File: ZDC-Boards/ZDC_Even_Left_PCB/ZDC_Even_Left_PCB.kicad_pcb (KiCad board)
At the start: 2 copper layers, 202.6 x 643 mm, 103 parts

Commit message: Updated ZDC connectors to pad connections, v2.0
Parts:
- removed REF** (x2): PinHeader_2x25_P1.27mm_Horizontal, Connector_PinHeader_1.27mm:PinHeader_2x25_P1.27mm_Horizontal
- added J1: TE_5-104895-5_AMPMODU_50-50_2x25_P1.27mm_Horizontal_SMD, TE_AMPMODU:TE_5-104895-5_AMPMODU_50-50_2x25_P1.27mm_Horizontal_SMD, F.Cu at (48.8, -634.4)
- added J2: TE_5-104895-5_AMPMODU_50-50_2x25_P1.27mm_Horizontal_SMD, TE_AMPMODU:TE_5-104895-5_AMPMODU_50-50_2x25_P1.27mm_Horizontal_SMD, F.Cu at (146.4, -634.4)
- #MK1, #MK2: renamed from REF**20; footprint SiPM:S14160-1315PS_dimple_silkscreen_with_capacitor -> SiPM:S14160-1315PS_silkscreen_marker
- C0, C1, C10, C11, C12, C13, C14, C15, C16, C17, C18, C19, C2, C20, C21, C22, C23, C24, C25, C26, C27, C28, C29, C3, C30, C31, C32, C33, C34, C35, C36, C37, C38, C39, C4, C40, C41, C42, C43, C44, C45, C46, C47, C5, C6, C7, C8, C9: renamed from 10 nF
- renumbered REF**20 to D0, REF**20 to D1, REF**20 to D10, REF**20 to D11, REF**20 to D12, REF**20 to D13, REF**20 to D14, REF**20 to D15, REF**20 to D16, REF**20 to D17, REF**20 to D18, REF**20 to D19, REF**20 to D2, REF**20 to D20, REF**20 to D21, REF**20 to D22, REF**20 to D23, REF**20 to D24, REF**20 to D25, REF**20 to D26, REF**20 to D27, REF**20 to D28, REF**20 to D29, REF**20 to D3, REF**20 to D30, REF**20 to D31, REF**20 to D32, REF**20 to D33, REF**20 to D34, REF**20 to D35, REF**20 to D36, REF**20 to D37, REF**20 to D38, REF**20 to D39, REF**20 to D4, REF**20 to D40, REF**20 to D41, REF**20 to D42, REF**20 to D43, REF**20 to D44, REF**20 to D45, REF**20 to D46, REF**20 to D47, REF**20 to D5, REF**20 to D6, REF**20 to D7, REF**20 to D8, REF**20 to D9, REF** to J3, REF** to J4
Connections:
- C24 pad 1: K0 -> K24
- C25 pad 1: K1 -> K25
- C26 pad 1: K2 -> K26
- C27 pad 1: K3 -> K27
- C28 pad 1: K4 -> K28
- C29 pad 1: K5 -> K29
- C30 pad 1: K6 -> K30
- C31 pad 1: K7 -> K31
- C32 pad 1: K8 -> K32
- C33 pad 1: K9 -> K33
- C34 pad 1: K10 -> K34
- C35 pad 1: K11 -> K35
- C36 pad 1: K12 -> K36
- C37 pad 1: K13 -> K37
- C38 pad 1: K14 -> K38
- C39 pad 1: K15 -> K39
- C40 pad 1: K16 -> K40
- C41 pad 1: K17 -> K41
- C42 pad 1: K18 -> K42
- C43 pad 1: K19 -> K43
- C44 pad 1: K20 -> K44
- C45 pad 1: K21 -> K45
- C46 pad 1: K22 -> K46
- C47 pad 1: K23 -> K47
- D0 pad : LK -> LK1
- D0 pad 7: (no net) -> K0
- D0 pad 8: (no net) -> A0
- D0 pad 9: LA -> LA1
- D1 pad : LK -> LK1
- D1 pad 7: (no net) -> K1
- D1 pad 8: (no net) -> A1
- D1 pad 9: LA -> LA1
- D10 pad : LK -> LK1
- D10 pad 7: (no net) -> K10
- D10 pad 8: (no net) -> A10
- D10 pad 9: LA -> LA1
- D11 pad : LK -> LK1
- D11 pad 7: (no net) -> K11
- D11 pad 8: (no net) -> A11
- D11 pad 9: LA -> LA1
- D12 pad : LK -> LK1
- D12 pad 9: LA -> LA1
- D13 pad : LK -> LK1
- D13 pad 7: (no net) -> K13
- D13 pad 8: (no net) -> A13
- D13 pad 9: LA -> LA1
- D14 pad : LK -> LK1
- D14 pad 7: (no net) -> K14
- D14 pad 8: (no net) -> A14
- D14 pad 9: LA -> LA1
- D15 pad : LK -> LK1
- D15 pad 7: (no net) -> K15
- D15 pad 8: (no net) -> A15
- D15 pad 9: LA -> LA1
- D16 pad : LK -> LK1
- D16 pad 7: (no net) -> K16
- D16 pad 8: (no net) -> A16
- D16 pad 9: LA -> LA1
- D17 pad : LK -> LK1
- D17 pad 7: (no net) -> K17
- D17 pad 9: LA -> LA1
- D18 pad : LK -> LK1
- D18 pad 7: (no net) -> K18
- D18 pad 8: (no net) -> A18
- D18 pad 9: LA -> LA1
- D19 pad : LK -> LK1
- D19 pad 7: (no net) -> K19
- D19 pad 8: (no net) -> A19
- D19 pad 9: LA -> LA1
- D2 pad : LK -> LK1
- D2 pad 7: (no net) -> K2
- D2 pad 8: (no net) -> A2
- D2 pad 9: LA -> LA1
- D20 pad : LK -> LK1
- D20 pad 7: (no net) -> K20
- D20 pad 8: (no net) -> A20
- D20 pad 9: LA -> LA1
- D21 pad : LK -> LK1
- D21 pad 7: (no net) -> K21
- D21 pad 8: (no net) -> A21
- D21 pad 9: LA -> LA1
- D22 pad : LK -> LK1
- D22 pad 7: (no net) -> K22
- D22 pad 8: (no net) -> A22
- D22 pad 9: LA -> LA1
- D23 pad : LK -> LK1
- D23 pad 7: (no net) -> K23
- D23 pad 8: (no net) -> A23
- D23 pad 9: LA -> LA1
- D24 pad : LK -> LK2
- D24 pad 7: (no net) -> K24
- D24 pad 8: (no net) -> A24
- D24 pad 9: LA -> LA2
- D25 pad : LK -> LK2
- D25 pad 7: (no net) -> K25
- D25 pad 8: (no net) -> A25
- D25 pad 9: LA -> LA2
- D26 pad : LK -> LK2
- D26 pad 7: (no net) -> K26
- D26 pad 8: (no net) -> A26
- D26 pad 9: LA -> LA2
- D27 pad : LK -> LK2
- D27 pad 7: (no net) -> K27
- D27 pad 8: (no net) -> A27
- D27 pad 9: LA -> LA2
- D28 pad : LK -> LK2
- D28 pad 7: (no net) -> K28
- D28 pad 8: (no net) -> A28
- D28 pad 9: LA -> LA2
- D29 pad : LK -> LK2
- D29 pad 7: (no net) -> K29
- D29 pad 8: A5 -> A29
- D29 pad 9: LA -> LA2
- D3 pad : LK -> LK1
- D3 pad 7: (no net) -> K3
- D3 pad 8: (no net) -> A3
- D3 pad 9: LA -> LA1
- D30 pad : LK -> LK2
- D30 pad 7: (no net) -> K30
- D30 pad 8: (no net) -> A30
- D30 pad 9: LA -> LA2
- D31 pad : LK -> LK2
- D31 pad 7: (no net) -> K31
- D31 pad 8: (no net) -> A31
- D31 pad 9: LA -> LA2
- D32 pad : LK -> LK2
- D32 pad 7: (no net) -> K32
- D32 pad 8: (no net) -> A32
- D32 pad 9: LA -> LA2
- D33 pad : LK -> LK2
- D33 pad 7: (no net) -> K33
- D33 pad 8: (no net) -> A33
- D33 pad 9: LA -> LA2
- D34 pad : LK -> LK2
- D34 pad 7: (no net) -> K34
- D34 pad 8: (no net) -> A34
- D34 pad 9: LA -> LA2
- D35 pad : LK -> LK2
- D35 pad 7: (no net) -> K35
- D35 pad 8: (no net) -> A35
- D35 pad 9: LA -> LA2
- D36 pad : LK -> LK2
- D36 pad 7: K12 -> K36
- D36 pad 8: A12 -> A36
- D36 pad 9: LA -> LA2
- D37 pad : LK -> LK2
- D37 pad 7: (no net) -> K37
- D37 pad 8: (no net) -> A37
- D37 pad 9: LA -> LA2
- D38 pad : LK -> LK2
- D38 pad 7: (no net) -> K38
- D38 pad 8: (no net) -> A38
- D38 pad 9: LA -> LA2
- D39 pad : LK -> LK2
- D39 pad 7: (no net) -> K39
- D39 pad 8: (no net) -> A39
- D39 pad 9: LA -> LA2
- D4 pad : LK -> LK1
- D4 pad 7: (no net) -> K4
- D4 pad 8: (no net) -> A4
- D4 pad 9: LA -> LA1
- D40 pad : LK -> LK2
- D40 pad 7: (no net) -> K40
- D40 pad 8: (no net) -> A40
- D40 pad 9: LA -> LA2
- D41 pad : LK -> LK2
- D41 pad 7: (no net) -> K41
- D41 pad 8: A17 -> A41
- D41 pad 9: LA -> LA2
- D42 pad : LK -> LK2
- D42 pad 7: (no net) -> K42
- D42 pad 8: (no net) -> A42
- D42 pad 9: LA -> LA2
- D43 pad : LK -> LK2
- D43 pad 7: (no net) -> K43
- D43 pad 8: (no net) -> A43
- D43 pad 9: LA -> LA2
- D44 pad : LK -> LK2
- D44 pad 7: (no net) -> K44
- D44 pad 8: (no net) -> A44
- D44 pad 9: LA -> LA2
- D45 pad : LK -> LK2
- D45 pad 7: (no net) -> K45
- D45 pad 8: (no net) -> A45
- D45 pad 9: LA -> LA2
- D46 pad : LK -> LK2
- D46 pad 7: (no net) -> K46
- D46 pad 8: (no net) -> A46
- D46 pad 9: LA -> LA2
- D47 pad : LK -> LK2
- D47 pad 7: (no net) -> K47
- D47 pad 8: (no net) -> A47
- D47 pad 9: LA -> LA2
- D5 pad : LK -> LK1
- D5 pad 7: (no net) -> K5
- D5 pad 9: LA -> LA1
- D6 pad : LK -> LK1
- D6 pad 7: (no net) -> K6
- D6 pad 8: (no net) -> A6
- D6 pad 9: LA -> LA1
- D7 pad : LK -> LK1
- D7 pad 7: (no net) -> K7
- D7 pad 8: (no net) -> A7
- D7 pad 9: LA -> LA1
- D8 pad : LK -> LK1
- D8 pad 7: (no net) -> K8
- D8 pad 8: (no net) -> A8
- D8 pad 9: LA -> LA1
- D9 pad : LK -> LK1
- D9 pad 7: (no net) -> K9
- D9 pad 8: (no net) -> A9
- D9 pad 9: LA -> LA1
- J3 pad 1: LA -> LA1
- J3 pad 2: LK -> LK1
- J4 pad 1: LA -> LA2
- J4 pad 2: LK -> LK2
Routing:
- net LK: track 2631.7 -> 0.00 mm, vias 48 -> 0
- net LA: track 2524.0 -> 0.00 mm, vias 4 -> 0
- net LK1: track 0.00 -> 1315.8 mm, vias 0 -> 24
- net LK2: track 0.00 -> 1315.8 mm, vias 0 -> 24
- net LA2: track 0.00 -> 1265.0 mm, vias 0 -> 2
- net LA1: track 0.00 -> 1265.0 mm, vias 0 -> 2
- net A35: track 0.00 -> 657.6 mm
- net A47: track 0.00 -> 655.7 mm
- net A23: track 1310.2 -> 655.7 mm
- net K47: track 0.00 -> 643.2 mm, vias 0 -> 2
- net K23: track 1285.6 -> 643.2 mm, vias 4 -> 2
- net A11: track 1295.7 -> 657.6 mm
- net K11: track 1248.1 -> 622.9 mm, vias 4 -> 2
- net K35: track 0.00 -> 622.9 mm, vias 0 -> 2
- net A46: track 0.00 -> 610.5 mm
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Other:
- board text added: "TE 5-104895-5 (AMPMODU 50/50 R/A SMT)"
- board text added: "ZDC Even Left PCB v2.0 Designed by Sean Preins"
- board text removed: "ZDC Even Left PCB v1.0 Designed by Sean Preins"

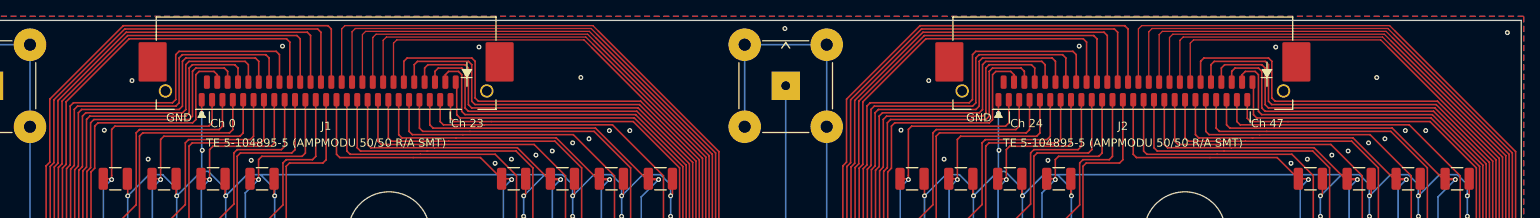
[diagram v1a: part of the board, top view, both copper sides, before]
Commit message: Updated ZDC boards to use new pin connectors that attach to crimped cables
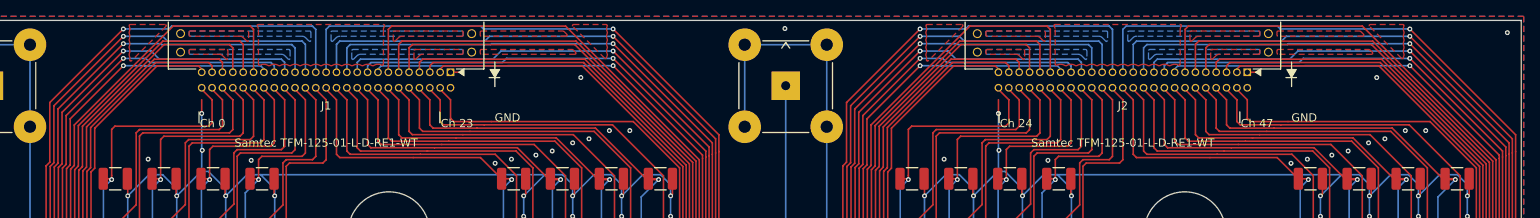
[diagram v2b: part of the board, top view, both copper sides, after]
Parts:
- J1, J2: value TE_5-104895-5_AMPMODU_50-50_2x25_P1.27mm_Horizontal_SMD -> Samtec_TFM-125-01-x-D-RE1-WT_2x25_P1.27mm_Horizontal; footprint TE_AMPMODU:TE_5-104895-5_AMPMODU_50-50_2x25_P1.27mm_Horizontal_SMD -> Samtec_TFM:Samtec_TFM-125-01-x-D-RE1-WT_2x25_P1.27mm_Horizontal
- moved #MK1 3.42 mm to (69.4, -636.0)
- moved #MK2 3.02 mm to (167.0, -636.0)
- moved J1 1.34 mm to (48.8, -635.7), turned to 0 degrees
- moved J2 1.34 mm to (146.4, -635.7), turned to 0 degrees
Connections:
- J1 pad 10: A3 -> K20
- J1 pad 11: K4 -> A19
- J1 pad 12: A4 -> K19
- J1 pad 13: K5 -> A18
- J1 pad 14: A5 -> K18
- J1 pad 15: K6 -> A17
- J1 pad 16: A6 -> K17
- J1 pad 17: K7 -> A16
- J1 pad 18: A7 -> K16
- J1 pad 19: K8 -> A15
- J1 pad 20: A8 -> K15
- J1 pad 21: K9 -> A14
- J1 pad 22: A9 -> K14
- J1 pad 23: K10 -> A13
- J1 pad 24: A10 -> K13
- J1 pad 25: K11 -> A12
- J1 pad 26: A11 -> K12
- J1 pad 27: K12 -> A11
- J1 pad 28: A12 -> K11
- J1 pad 29: K13 -> A10
- J1 pad 3: K0 -> A23
- J1 pad 30: A13 -> K10
- J1 pad 31: K14 -> A9
- J1 pad 32: A14 -> K9
- J1 pad 33: K15 -> A8
- J1 pad 34: A15 -> K8
- J1 pad 35: K16 -> A7
- J1 pad 36: A16 -> K7
- J1 pad 37: K17 -> A6
- J1 pad 38: A17 -> K6
- J1 pad 39: K18 -> A5
- J1 pad 4: A0 -> K23
- J1 pad 40: A18 -> K5
- J1 pad 41: K19 -> A4
- J1 pad 42: A19 -> K4
- J1 pad 43: K20 -> A3
- J1 pad 44: A20 -> K3
- J1 pad 45: K21 -> A2
- J1 pad 46: A21 -> K2
- J1 pad 47: K22 -> A1
- J1 pad 48: A22 -> K1
- J1 pad 49: K23 -> A0
- J1 pad 5: K1 -> A22
- J1 pad 50: A23 -> K0
- J1 pad 6: A1 -> K22
- J1 pad 7: K2 -> A21
- J1 pad 8: A2 -> K21
- J1 pad 9: K3 -> A20
- J2 pad 10: A27 -> K44
- J2 pad 11: K28 -> A43
- J2 pad 12: A28 -> K43
- J2 pad 13: K29 -> A42
- J2 pad 14: A29 -> K42
- J2 pad 15: K30 -> A41
- J2 pad 16: A30 -> K41
- J2 pad 17: K31 -> A40
- J2 pad 18: A31 -> K40
- J2 pad 19: K32 -> A39
- J2 pad 20: A32 -> K39
- J2 pad 21: K33 -> A38
- J2 pad 22: A33 -> K38
- J2 pad 23: K34 -> A37
- J2 pad 24: A34 -> K37
- J2 pad 25: K35 -> A36
- J2 pad 26: A35 -> K36
- J2 pad 27: K36 -> A35
- J2 pad 28: A36 -> K35
- J2 pad 29: K37 -> A34
- J2 pad 3: K24 -> A47
- J2 pad 30: A37 -> K34
- J2 pad 31: K38 -> A33
- J2 pad 32: A38 -> K33
- J2 pad 33: K39 -> A32
- J2 pad 34: A39 -> K32
- J2 pad 35: K40 -> A31
- J2 pad 36: A40 -> K31
- J2 pad 37: K41 -> A30
- J2 pad 38: A41 -> K30
- J2 pad 39: K42 -> A29
- J2 pad 4: A24 -> K47
- J2 pad 40: A42 -> K29
- J2 pad 41: K43 -> A28
- J2 pad 42: A43 -> K28
- J2 pad 43: K44 -> A27
- J2 pad 44: A44 -> K27
- J2 pad 45: K45 -> A26
- J2 pad 46: A45 -> K26
- J2 pad 47: K46 -> A25
- J2 pad 48: A46 -> K25
- J2 pad 49: K47 -> A24
- J2 pad 5: K25 -> A46
- J2 pad 50: A47 -> K24
- J2 pad 6: A25 -> K46
- J2 pad 7: K26 -> A45
- J2 pad 8: A26 -> K45
- J2 pad 9: K27 -> A44
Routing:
- net A6: track 402.0 -> 392.3 mm, vias 0 -> 1
- net A30: track 402.0 -> 392.3 mm, vias 0 -> 1
- net A7: track 452.1 -> 444.3 mm, vias 0 -> 1
- net A31: track 452.1 -> 444.3 mm, vias 0 -> 1
- net A8: track 503.5 -> 496.3 mm, vias 0 -> 1
- net A32: track 503.5 -> 496.3 mm, vias 0 -> 1
- net A2: track 195.7 -> 189.7 mm
- net A26: track 195.7 -> 189.7 mm
- net A9: track 554.9 -> 549.1 mm, vias 0 -> 1
- net A33: track 554.9 -> 549.1 mm, vias 0 -> 1
- net A1: track 144.1 -> 138.3 mm
- net A25: track 144.1 -> 138.3 mm
- net A0: track 93.1 -> 87.6 mm
- net A24: track 93.1 -> 87.6 mm
- net A10: track 606.3 -> 601.1 mm, vias 0 -> 1
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- added copper zone on B.Cu, net (none)
- added copper zone on F.Cu, net (none)
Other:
- board text added: "Samtec TFM-125-01-L-D-RE1-WT"
- board text removed: "TE 5-104895-5 (AMPMODU 50/50 R/A SMT)"
